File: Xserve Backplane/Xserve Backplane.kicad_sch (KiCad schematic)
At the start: 46 parts, among them CN1 0678008025_SATA_Conn, CN2 0678008025_SATA_Conn, CN3 0678008025_SATA_Conn, J2 Conn_02x03_Odd_Even, J3 1888019-2, J4 SATA_Combo, J5 SATA_Combo, J6 SATA_Combo, Q1 Q_NMOS_DGS, Q2 Q_NMOS_DGS, Q3 Q_NMOS_DGS, Q4 Q_NMOS_DGS, Q5 Q_NMOS_DGS, Q6 Q_NMOS_DGS, U1 BD9E302EFJ-E2

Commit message: "Ran DRC, changed mosfet footprint"
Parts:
- L1: value 680 uH -> 15 uH; footprint KiCADs:60B474C -> Inductor_SMD:L_12x12mm_H8mm; Spice_Model (none) -> 15u; Spice_Netlist_Enabled (none) -> Y; Spice_Primitive (none) -> L
- Q1, Q2, Q3, Q4, Q5, Q6: symbol Device:Q_NMOS_DGS -> Device:Q_NMOS_SGD
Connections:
- net ACT_1: now also Q5.3 (D); no longer Q5.1 (D)
- net ACT_2: now also Q6.3 (D); no longer Q6.1 (D)
- net ACT_3: now also Q2.3 (D); no longer Q2.1 (D)
- net Earth: now also Q1.1 (S), Q2.1 (S), Q3.1 (S), Q4.1 (S), Q5.1 (S), Q6.1 (S); no longer Q1.3 (S), Q2.3 (S), Q3.3 (S), Q4.3 (S), Q5.3 (S), Q6.3 (S)
- net at C8.1, Q2.2 (G), R5.2: now also Q1.3 (D); no longer Q1.1 (D)
- net at C16.1, Q5.2 (G), R8.2: now also Q3.3 (D); no longer Q3.1 (D)
- net at C17.1, Q6.2 (G), R9.2: now also Q4.3 (D); no longer Q4.1 (D)
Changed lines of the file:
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@@
     (pin "2")
   )
-  (symbol (lib_id "Device:Q_NMOS_DGS") (at 271.78 238.125 0) (unit 1)
+  (symbol (lib_id "Device:Q_NMOS_SGD") (at 271.78 238.125 0) (unit 1)
     (in_bom yes) (on_board yes) (fields_autoplaced)
     (property "Reference" "Q2" (id 0) (at 278.13 236.8549 0)
@@
     (pin "1")
   )
-  (symbol (lib_id "Device:Q_NMOS_DGS") (at 271.78 89.535 0) (unit 1)
+  (symbol (lib_id "Device:Q_NMOS_SGD") (at 271.78 89.535 0) (unit 1)
     (in_bom yes) (on_board yes) (fields_autoplaced)
     (property "Reference" "Q5" (id 0) (at 278.13 88.2649 0)
@@
       (effects (font (size 1.27 1.27)) hide)
     )
-    (property "Datasheet" "~" (id 3) (at 55.88 29.845 0)
+    (property "Datasheet" "https://www.molex.com/pdm_docs/pk/PK-5569-002.pdf" (id 3) (at 55.88 29.845 0)
       (effects (font (size 1.27 1.27)) hide)
     )
@@
     (pin "1")
   )
-  (symbol (lib_id "Device:Q_NMOS_DGS") (at 256.54 104.775 0) (unit 1)
+  (symbol (lib_id "Device:Q_NMOS_SGD") (at 256.54 104.775 0) (unit 1)
     (in_bom yes) (on_board yes) (fields_autoplaced)
     (property "Reference" "Q3" (id 0) (at 262.89 103.5049 0)
@@
   (symbol (lib_id "power:GND") (at 243.84 264.16 0) (unit 1)
     (in_bom yes) (on_board yes) (fields_autoplaced)
-    (property "Reference" "#PWR?" (id 0) (at 243.84 270.51 0)
+    (property "Reference" "#PWR0124" (id 0) (at 243.84 270.51 0)
       (effects (font (size 1.27 1.27)) hide)
     )
@@
     (pin "2")
   )
-  (symbol (lib_id "Device:Q_NMOS_DGS") (at 256.54 253.365 0) (unit 1)
+  (symbol (lib_id "Device:Q_NMOS_SGD") (at 256.54 253.365 0) (unit 1)
     (in_bom yes) (on_board yes) (fields_autoplaced)
     (property "Reference" "Q1" (id 0) (at 262.89 252.0949 0)
@@
     (in_bom yes) (on_board yes) (fields_autoplaced)
     (property "Reference" "L1" (id 0) (at 107.95 64.77 90))
-    (property "Value" "680 uH" (id 1) (at 107.95 67.31 90))
-    (property "Footprint" "KiCADs:60B474C" (id 2) (at 107.95 69.85 0)
-      (effects (font (size 1.27 1.27)) hide)
-    )
-    (property "Datasheet" "https://www.digikey.com/en/products/detail/murata-power-solutions-inc/60B684C/3178537" (id 3) (at 107.95 69.85 0)
-      (effects (font (size 1.27 1.27)) hide)
-    )
-    (pin "1")
-    (pin "2")
-  )
-  (symbol (lib_id "Device:Q_NMOS_DGS") (at 256.54 177.165 0) (unit 1)
+    (property "Value" "15 uH" (id 1) (at 107.95 67.31 90))
+    (property "Footprint" "Inductor_SMD:L_12x12mm_H8mm" (id 2) (at 107.95 69.85 0)
+      (effects (font (size 1.27 1.27)) hide)
+    )
+    (property "Datasheet" "https://www.digikey.com/en/products/detail/w%C3%BCrth-elektronik/744770115/1638630" (id 3) (at 107.95 69.85 0)
+      (effects (font (size 1.27 1.27)) hide)
+    )
+    (property "Spice_Primitive" "L" (id 4) (at 107.95 69.85 0)
+      (effects (font (size 1.27 1.27)) hide)
+    )
+    (property "Spice_Model" "15u" (id 5) (at 107.95 69.85 0)
+      (effects (font (size 1.27 1.27)) hide)
+    )
+    (property "Spice_Netlist_Enabled" "Y" (id 6) (at 107.95 69.85 0)
+      (effects (font (size 1.27 1.27)) hide)
+    )
+    (pin "1")
+    (pin "2")
+  )
+  (symbol (lib_id "Device:Q_NMOS_SGD") (at 256.54 177.165 0) (unit 1)
     (in_bom yes) (on_board yes) (fields_autoplaced)
     (property "Reference" "Q4" (id 0) (at 262.89 175.8949 0)
@@
     (pin "1")
   )
-  (symbol (lib_id "Device:Q_NMOS_DGS") (at 271.78 161.925 0) (unit 1)
+  (symbol (lib_id "Device:Q_NMOS_SGD") (at 271.78 161.925 0) (unit 1)
     (in_bom yes) (on_board yes) (fields_autoplaced)
     (property "Reference" "Q6" (id 0) (at 278.13 160.6549 0)
@@
       (reference "#PWR0123") (unit 1) (value "GND") (footprint "")
     )
+    (path "/81cb9056-95ce-4279-9403-5c396e1a0e3a"
+      (reference "#PWR0124") (unit 1) (value "GND") (footprint "")
+    )
     (path "/0ac0e2dd-5e8a-4232-ba74-6db4ea08c2fa"
       (reference "#PWR0125") (unit 1) (value "GND") (footprint "")
@@
       (reference "#PWR0135") (unit 1) (value "GND") (footprint "")
     )
-    (path "/81cb9056-95ce-4279-9403-5c396e1a0e3a"
-      (reference "#PWR?") (unit 1) (value "GND") (footprint "")
-    )
     (path "/39d3dbc2-fa82-479b-842e-f88fab4b8d1b"
       (reference "C1") (unit 1) (value "10uF") (footprint "Capacitor_SMD:C_0603_1608Metric_Pad1.08x0.95mm_HandSolder")
@@
     )
     (path "/e3455460-81d0-44e4-8aea-1f5e9c19731b"
-      (reference "L1") (unit 1) (value "680 uH") (footprint "KiCADs:60B474C")
+      (reference "L1") (unit 1) (value "15 uH") (footprint "Inductor_SMD:L_12x12mm_H8mm")
     )
     (path "/c9044aa6-2851-491b-bd06-39ba6f744a82"

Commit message: Creatd Ampehnol SAS connector footprint and implemented in schematic. Began implementation in layout.
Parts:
- removed J4, J5, J6: SATA_Combo, Connector_SATA_SAS:SATA_Amphenol_10029364-001LF_Horizontal, symbol KiCADs:SATA_Combo
- added J1, J7, J8: ~, KiCADs:10124274-001TRLF, symbol KiCADs:10124274-001TRLF
- L1: Spice_Model 15u -> (none); Spice_Netlist_Enabled Y -> (none); Spice_Primitive L -> (none)
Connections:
- net 12V: now also J1.P13 (12V), J1.P14 (12V), J1.P15 (12V), J7.P13 (12V), J7.P14 (12V), J7.P15 (12V), J8.P13 (12V), J8.P14 (12V), J8.P15 (12V)
- net 3V3: now also J1.P1 (3.3V), J1.P2 (3.3V), J1.P3 (3.3V), J7.P1 (3.3V), J7.P2 (3.3V), J7.P3 (3.3V), J8.P1 (3.3V), J8.P2 (3.3V), J8.P3 (3.3V)
- net 5V: now also J1.P7 (5V), J1.P8 (5V), J1.P9 (5V), J7.P7 (5V), J7.P8 (5V), J7.P9 (5V), J8.P7 (5V), J8.P8 (5V), J8.P9 (5V)
- net A1+: now also J1.S2 (RP+)
- net A1-: now also J1.S3 (RP-)
- net A2+: now also J7.S2 (RP+)
- net A2-: now also J7.S3 (RP-)
- net A3+: now also J8.S2 (RP+)
- net A3-: now also J8.S3 (RP-)
- net ACT_1: now also J1.P11 (GND/LED)
- net ACT_2: now also J7.P11 (GND/LED)
- net ACT_3: now also J8.P11 (GND/LED)
- net B1+: now also J1.S6 (TP+)
- net B1-: now also J1.S5 (TP-)
- net B2+: now also J7.S6 (TP+)
- net B2-: now also J7.S5 (TP-)
- net B3+: now also J8.S6 (TP+)
- net B3-: now also J8.S5 (TP-)
- net Earth: now also J1.P10 (GND), J1.P12 (GND), J1.P4 (GND), J1.P5 (GND), J1.P6 (GND), J1.S1 (GND), J1.S4 (GND), J1.S7 (GND), J7.P10 (GND), J7.P12 (GND), J7.P4 (GND), J7.P5 (GND), J7.P6 (GND), J7.S1 (GND), J7.S4 (GND), J7.S7 (GND), J8.P10 (GND), J8.P12 (GND), J8.P4 (GND), J8.P5 (GND), J8.P6 (GND), J8.S1 (GND), J8.S4 (GND), J8.S7 (GND)
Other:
- moved on the sheet: C1, C10, C11, C12, C13, C14, C15, C16, C17, C2, C3, C4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

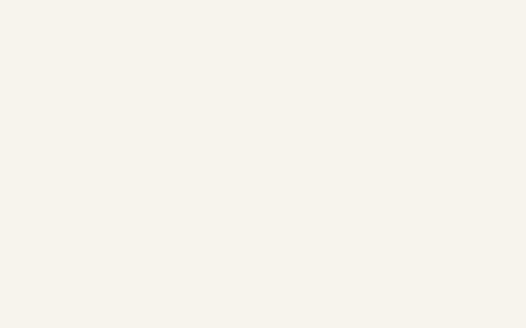
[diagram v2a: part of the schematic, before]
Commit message: created SAS connector footprint and added to layout. next step is routing with new connector
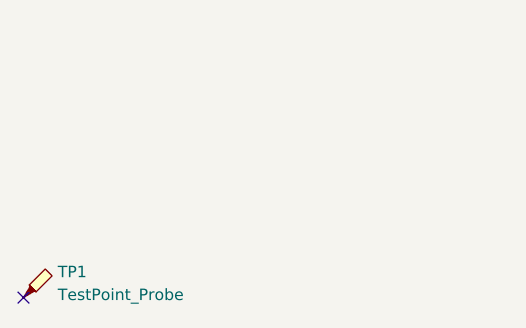
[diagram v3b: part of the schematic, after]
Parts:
- added TP1: TestPoint_Probe, KiCADs:TheColonelCu, symbol Connector:TestPoint_Probe
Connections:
- no-connect marks 12 -> 13
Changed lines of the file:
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@@
   (no_connect (at 187.96 248.92))
   (no_connect (at 157.48 251.46))
+  (no_connect (at 15.24 402.59))
   (no_connect (at 151.13 264.16))
   (no_connect (at 187.96 246.38))
@@
         )
       )
+    )
+  )
+  (symbol (lib_id "Connector:TestPoint_Probe") (at 15.24 402.59 0) (unit 1)
+    (in_bom yes) (on_board yes) (dnp no)
+    (property "Reference" "TP1" (at 19.05 399.7325 0)
+      (effects (font (size 1.27 1.27)) (justify left))
+    )
+    (property "Value" "TestPoint_Probe" (at 19.05 402.2725 0)
+      (effects (font (size 1.27 1.27)) (justify left))
+    )
+    (property "Footprint" "KiCADs:TheColonelCu" (at 20.32 402.59 0)
+      (effects (font (size 1.27 1.27)) hide)
+    )
+    (property "Datasheet" "~" (at 20.32 402.59 0)
+      (effects (font (size 1.27 1.27)) hide)
+    )
+    (pin "1")
+    (instances
+      (project "Xserve Backplane"
+        (path "/111912a3-65d6-4c33-9374-66c89bdc7744"
+          (reference "TP1") (unit 1)
+        )
+      )

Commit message: rough pass at SAS connector layout and some DRC fixes, this board should be manufacturable.
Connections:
- net Earth: now also U1.9 (EPAD); no longer U1.EPAD
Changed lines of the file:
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@@
     (pin "7")
     (pin "8")
-    (pin "EPAD")
+    (pin "9")
     (instances
       (project "Xserve Backplane"

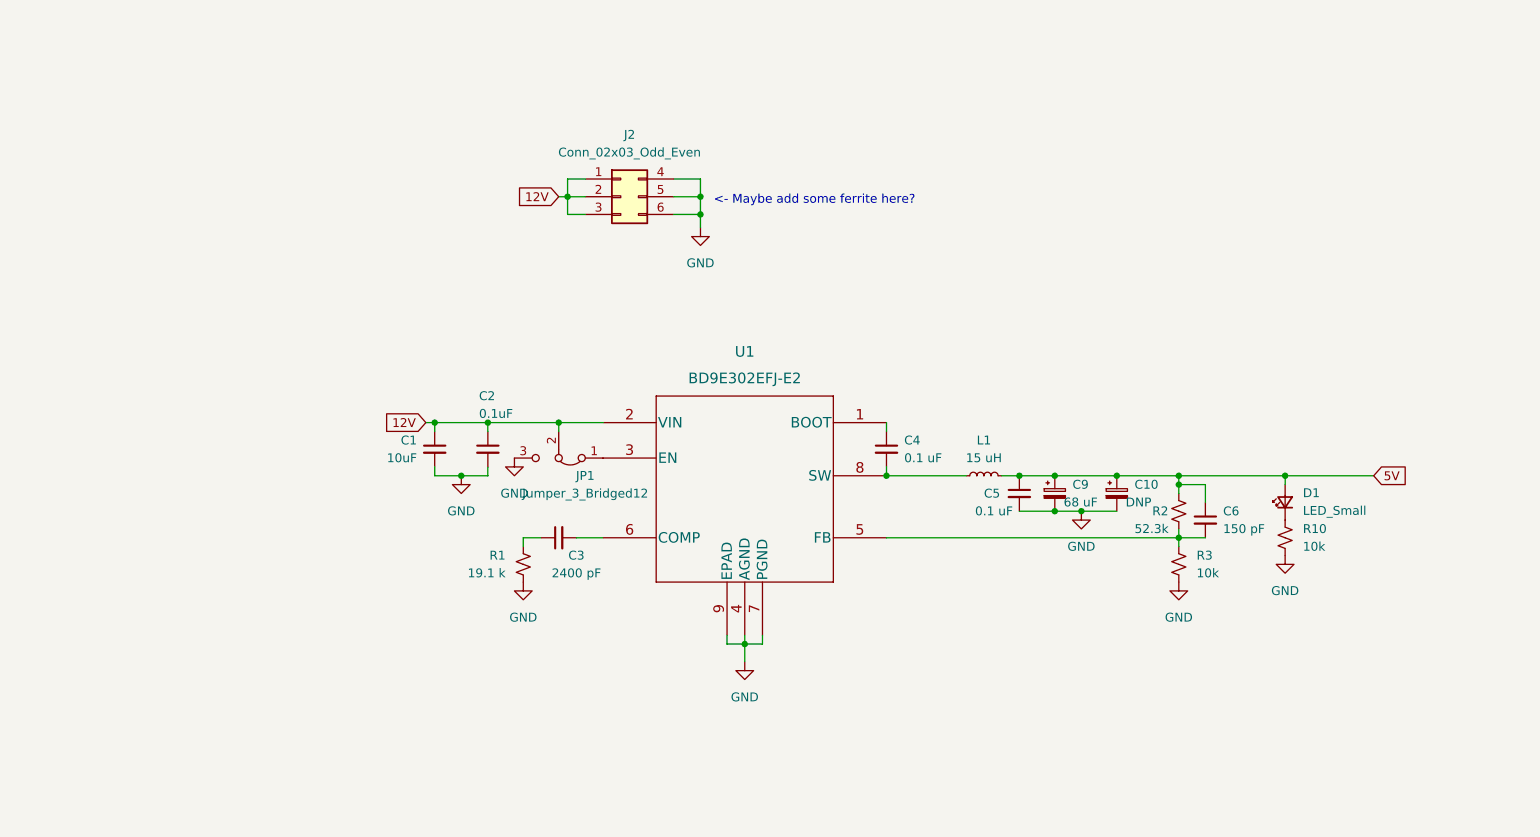
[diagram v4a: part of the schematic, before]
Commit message: misinterpreted JLC's via size capabilities. increased minimum via to 0.46 mm to comply with their requirements.
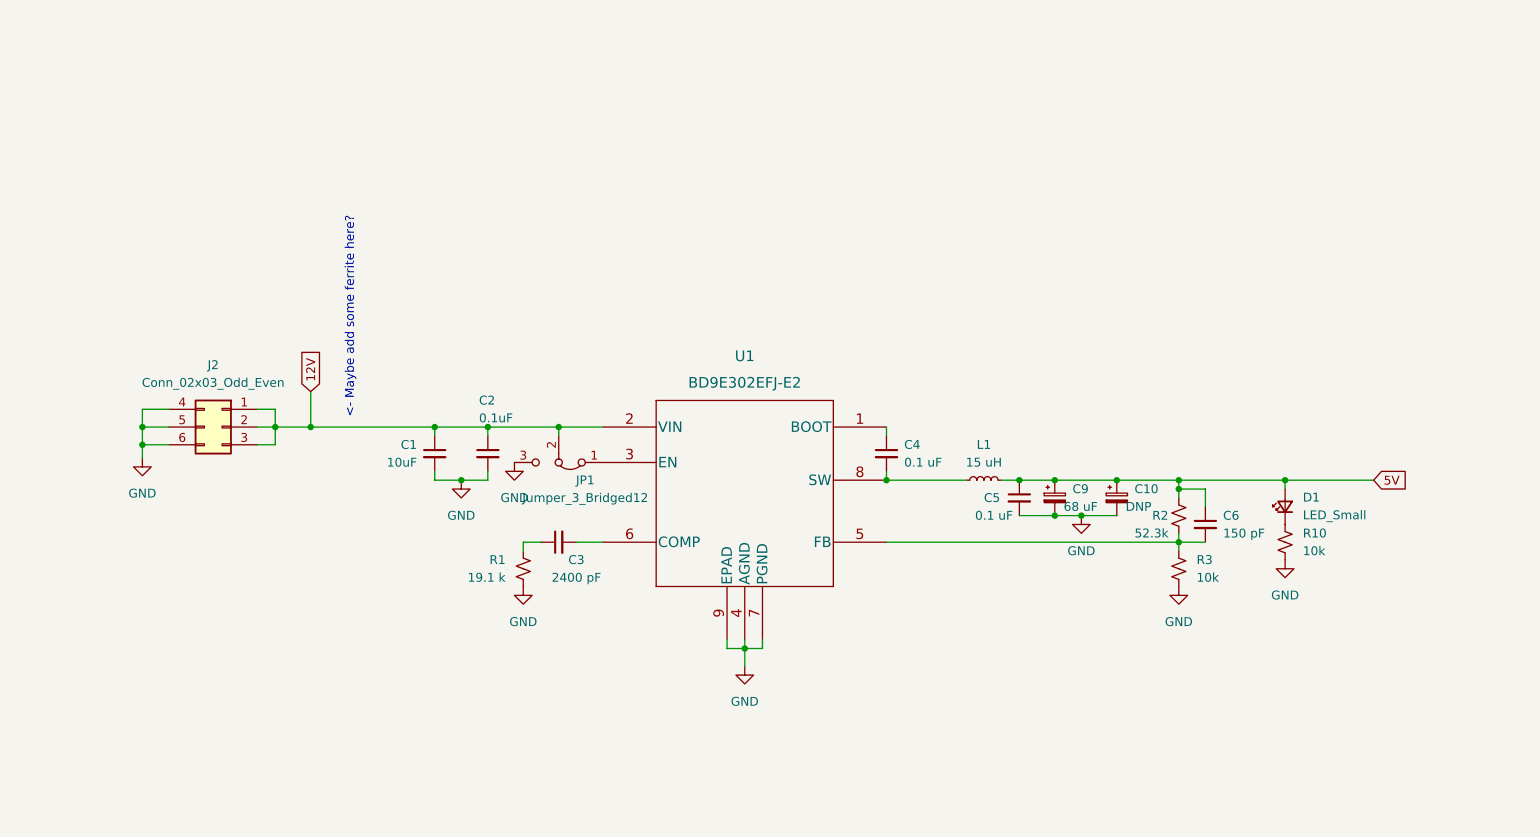
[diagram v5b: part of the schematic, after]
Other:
- moved on the sheet: C1, C10, C2, C3, C4, C5, C6, C9, D1, J2, JP1, L1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
